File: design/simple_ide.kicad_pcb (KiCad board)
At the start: 4 copper layers, 41 x 100 mm, 14 parts, among them IC1 ATF22V10C-15PU, IC2 ATF22V10C-15PU, IC3 74ACT245, IC4 74ACT245, J2 Conn_02x22_Odd_Even

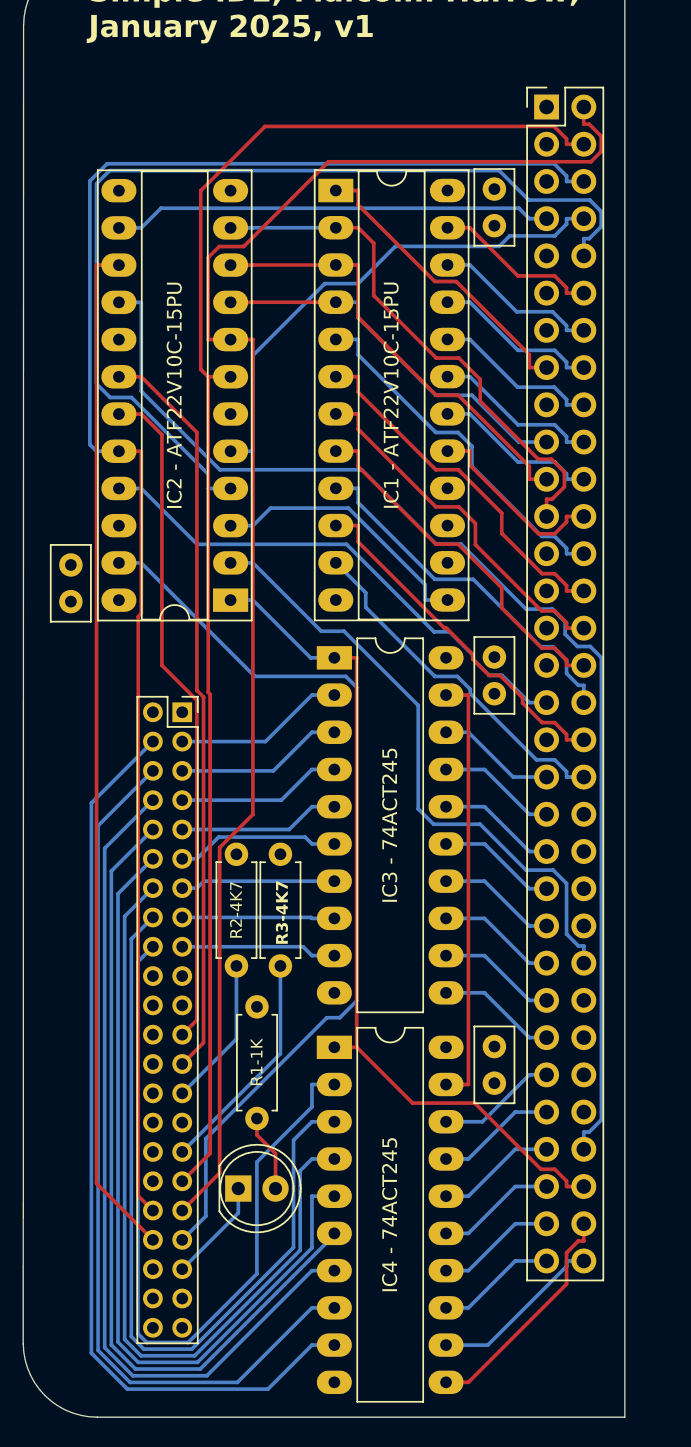
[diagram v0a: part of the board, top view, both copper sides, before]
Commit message: Recheck WinCUPL against design
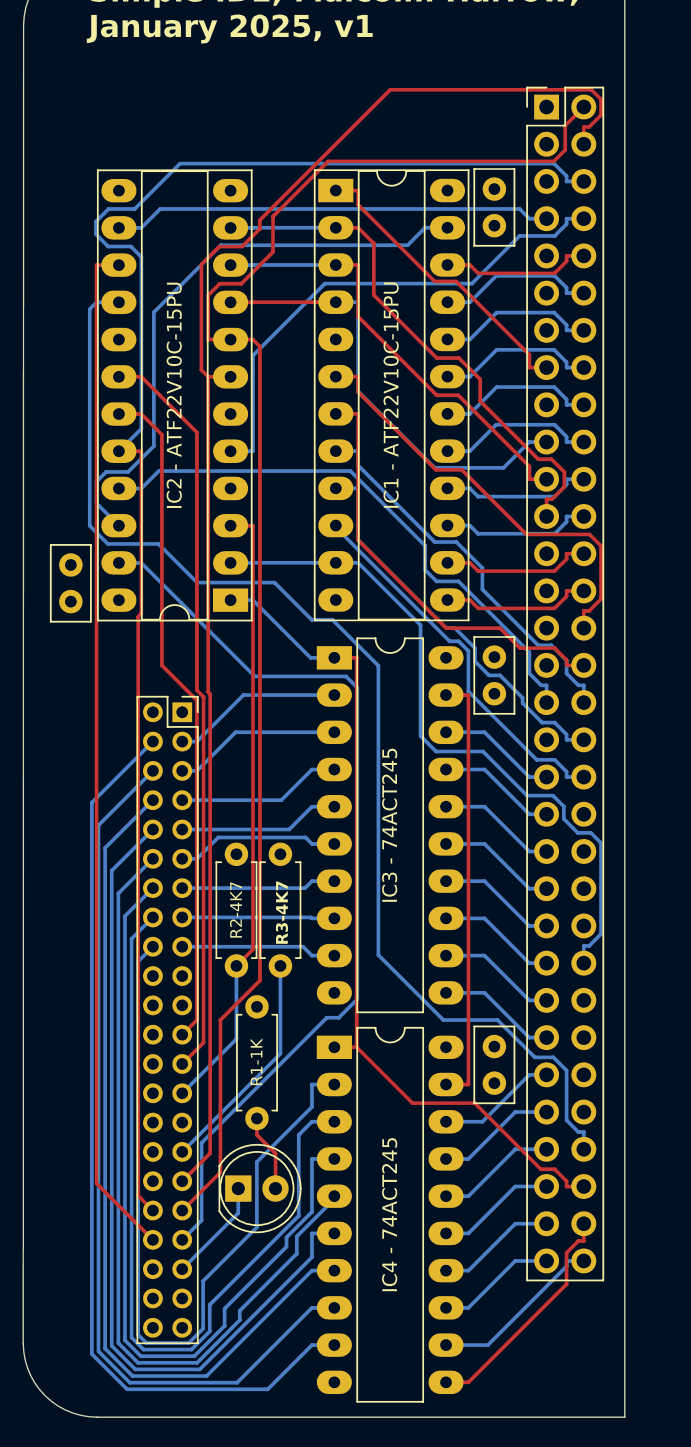
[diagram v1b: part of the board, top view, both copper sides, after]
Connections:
- IC1 pad 10: A18 -> A19
- IC1 pad 11: A19 -> AS
- IC1 pad 13: ~{IDECS} -> A14
- IC1 pad 14: unconnected-(IC1-I/O_1-Pad14) -> A13
- IC1 pad 15: unconnected-(IC1-I/O_2-Pad15) -> A12
- IC1 pad 16: unconnected-(IC1-I/O_3-Pad16) -> A11
- IC1 pad 17: A12 -> A10
- IC1 pad 18: A11 -> A9
- IC1 pad 19: A10 -> A8
- IC1 pad 20: A9 -> A7
- IC1 pad 21: A8 -> A6
- IC1 pad 22: A7 -> A5
- IC1 pad 23: A6 -> ~{IDECS}
- IC1 pad 5: A13 -> unconnected-(IC1-IN_3-Pad5)
- IC1 pad 6: A14 -> A15
- IC1 pad 7: A15 -> A16
- IC1 pad 8: A16 -> A17
- IC1 pad 9: A17 -> A18
- IC2 pad 22: unconnected-(IC2-I/O_9-Pad22) -> ~{IDECS}
- IC2 pad 3: ~{IDECS} -> IDERDY
- IC2 pad 4: A5 -> unconnected-(IC2-IN/PD-Pad4)
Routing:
- net A5: track 66.0 -> 10.2 mm
- net IDERDY: track 10.2 -> 42.3 mm
- net ~{IDECS}: track 18.5 -> 40.1 mm
- net A14: track 24.6 -> 10.2 mm
- net A13: track 24.6 -> 10.2 mm
- net A15: track 24.7 -> 29.8 mm
- net AS: track 42.3 -> 47.0 mm
- net A16: track 24.6 -> 29.3 mm
- net FC0: track 26.1 -> 30.6 mm
- net UDS: track 35.4 -> 38.7 mm
- net A2: track 98.8 -> 101.7 mm
- net A18: track 24.2 -> 27.0 mm
- net A12: track 12.9 -> 10.2 mm
- net A1: track 103.6 -> 101.2 mm
- net A19: track 23.9 -> 25.9 mm
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
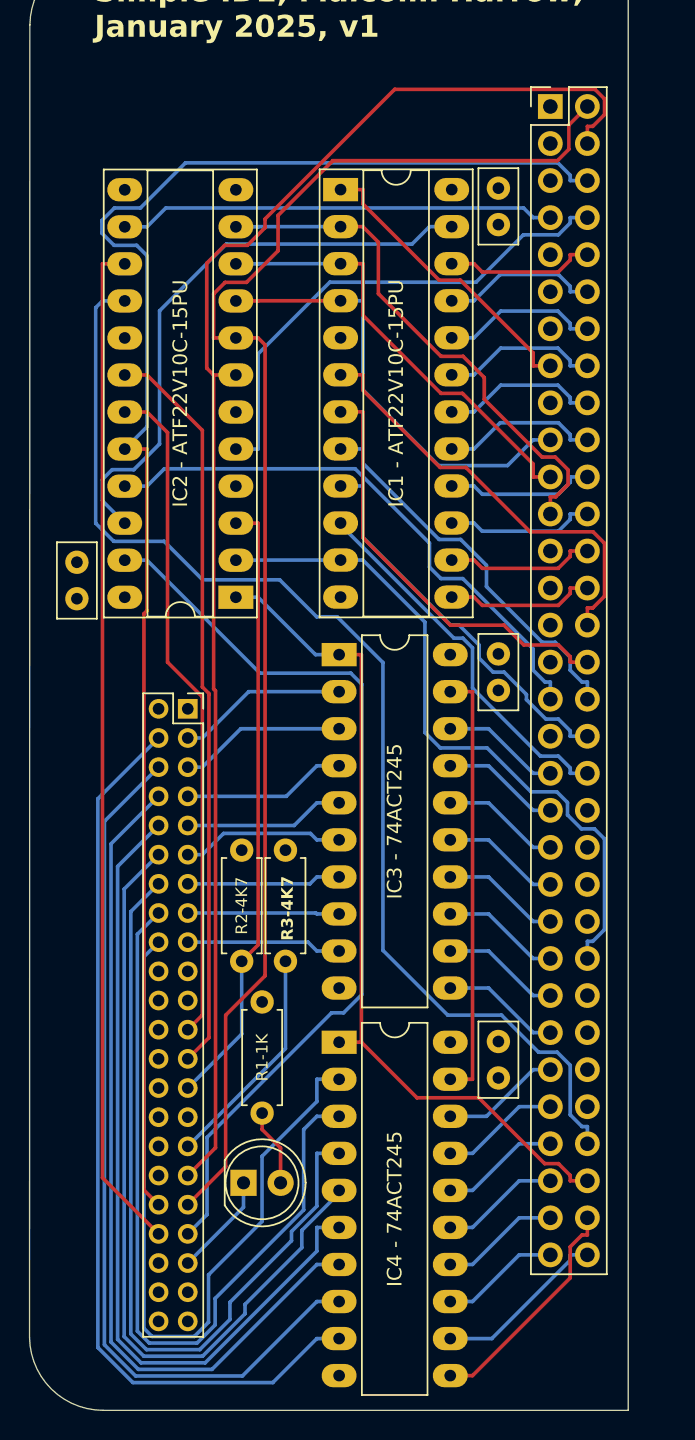
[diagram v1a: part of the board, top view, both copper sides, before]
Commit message: Compile Wincuple and reroute pins to ensure outputs on output pins
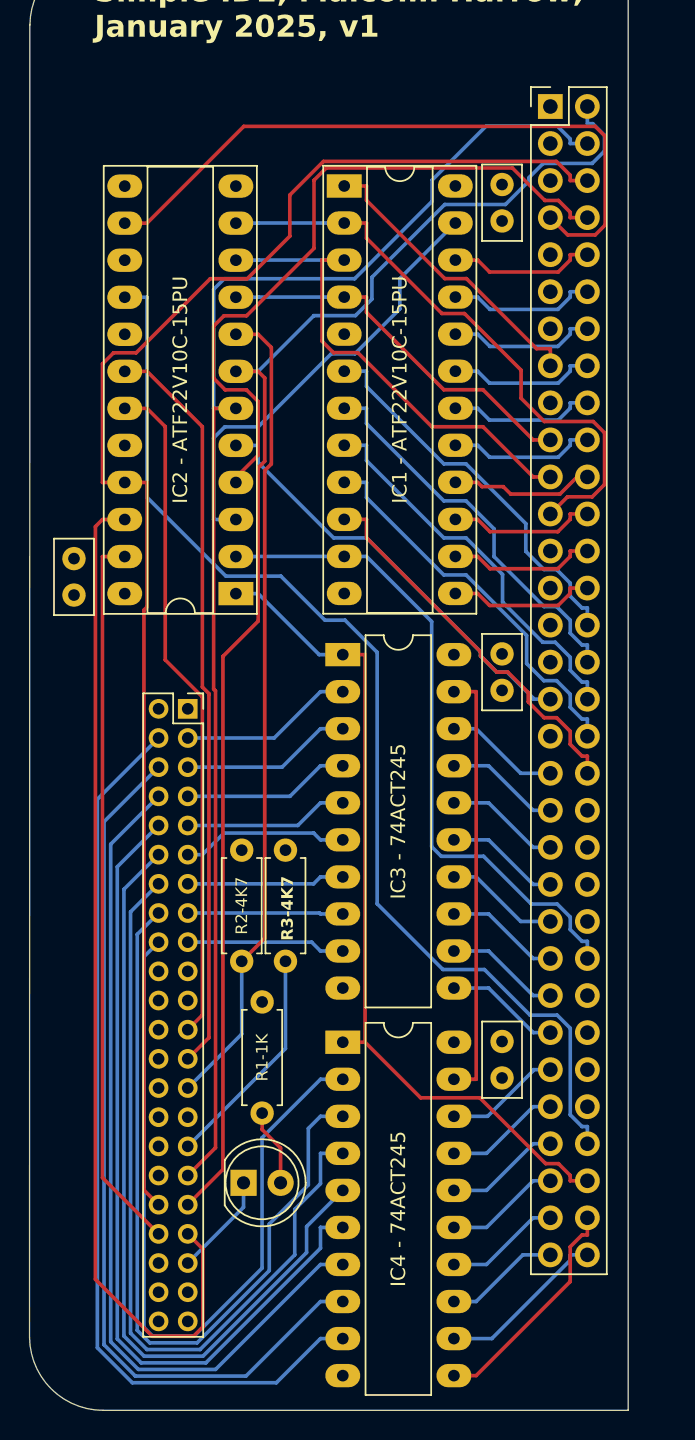
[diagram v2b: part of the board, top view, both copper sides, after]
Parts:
- moved C4 0.35 mm to (175.3, 51.0)
- moved IC1 0.35 mm to (164.5, 51.0)
- moved C3 0.32 mm to (146.0, 79.1)
- moved C1 0.25 mm to (175.3, 109.7)
- moved C2 0.25 mm to (175.3, 83.1)
- moved IC2 0.25 mm to (157.1, 79.0)
- moved IC3 0.25 mm to (164.4, 83.2)
- moved IC4 0.25 mm to (164.4, 109.8)
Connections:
- IC2 pad 13: IDESEL -> unconnected-(IC2-IN_10-Pad13)
- IC2 pad 15: ~{IDECS1} -> unconnected-(IC2-I/O_2-Pad15)
- IC2 pad 20: A3 -> IDESEL
- IC2 pad 21: UDS -> A3
- IC2 pad 22: ~{IDECS} -> ~{IDECS0}
- IC2 pad 23: ~{IDECS0} -> ~{IDECS1}
- IC2 pad 3: IDERDY -> ~{IDECS}
- IC2 pad 4: unconnected-(IC2-IN/PD-Pad4) -> A4
- IC2 pad 5: A4 -> UDS
- IC2 pad 6: unconnected-(IC2-IN_4-Pad6) -> A2
- IC2 pad 7: A2 -> A1
- IC2 pad 8: A1 -> IDERDY
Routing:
- net ~{IDECS1}: track 69.6 -> 49.6 mm
- net VPA: track 30.0 -> 46.6 mm
- net IDERDY: track 42.3 -> 56.0 mm
- net A4: track 34.7 -> 47.9 mm
- net ~{IDECS}: track 40.1 -> 31.0 mm
- net UDS: track 38.7 -> 29.7 mm
- net ~{IDECS0}: track 62.9 -> 69.9 mm
- net A3: track 108.0 -> 102.6 mm
- net A2: track 101.7 -> 96.5 mm
- net FC2: track 36.4 -> 41.1 mm
- net DTACK: track 82.5 -> 78.1 mm
- net FC0: track 30.6 -> 26.2 mm
- net A1: track 101.2 -> 97.3 mm
- net FC1: track 30.2 -> 34.0 mm
- net A15: track 29.8 -> 26.8 mm
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
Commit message: Start work on v2
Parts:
- removed D2: LED, LED_THT:LED_D5.0mm
- removed R1: 1K, Resistor_THT:R_Axial_DIN0207_L6.3mm_D2.5mm_P7.62mm_Horizontal
- removed R2, R3: 4K7, Resistor_THT:R_Axial_DIN0207_L6.3mm_D2.5mm_P7.62mm_Horizontal
- IC3, IC4: value 74ACT245 -> 74245
- moved C3 31.8 mm to (160.7, 51.0), turned to -90 degrees
- moved IC2 28.9 mm to (149.6, 51.0), turned to 0 degrees
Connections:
- IC2 pad 10: FC1 -> unconnected-(IC2-IN_8-Pad10)
- IC2 pad 11: FC2 -> unconnected-(IC2-IN_9-Pad11)
- IC2 pad 13: unconnected-(IC2-IN_10-Pad13) -> A2
- IC2 pad 14: VPA -> A1
- IC2 pad 6: A2 -> unconnected-(IC2-IN_4-Pad6)
- IC2 pad 7: A1 -> unconnected-(IC2-IN_5-Pad7)
- IC2 pad 8: IDERDY -> unconnected-(IC2-IN_6-Pad8)
- IC2 pad 9: FC0 -> unconnected-(IC2-IN_7-Pad9)
- IC3 pad 19: IDEBUF -> ~{IDEBUF}
- IC4 pad 19: IDEBUF -> ~{IDEBUF}
- J2 pad 1: ~{RESET} -> RESET
- J2 pad 27: IDERDY -> unconnected-(J2-Pin_27-Pad27)
- J2 pad 31: INTRQ -> unconnected-(J2-Pin_31-Pad31)
- J2 pad 39: ~{DASP} -> unconnected-(J2-Pin_39-Pad39)
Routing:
- net RESET: track 0.00 -> 69.3 mm, vias 0 -> 1
- net IDERDY: track 56.0 -> 0.00 mm
- net ~{IDEBUF}: track 0.00 -> 54.3 mm
- net VPA: track 46.6 -> 0.00 mm
- net RW: track 58.1 -> 92.4 mm
- net IDEBUF: track 29.6 -> 0.00 mm
- net A1: track 97.3 -> 126.8 mm
- net AS: track 45.8 -> 71.9 mm
- net ~{IDECS1}: track 49.6 -> 73.7 mm
- net DTACK: track 78.1 -> 59.7 mm
- net INTRQ: track 15.5 -> 0.00 mm
- net A2: track 96.5 -> 111.6 mm
- net FC2: track 41.1 -> 27.8 mm
- net UDS: track 29.7 -> 42.2 mm
- net A3: track 102.6 -> 94.1 mm
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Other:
- board text added: "< 1"
- board text added: "DID YOU CHANGE A2 and A1 in PLD ???"
- board text added: "IC1"
- board text added: "IC2"
- board text added: "KEY --->"
- board text added: "Simple IDE, Malcolm Harrow, February 2025, v2"
- board text removed: "Simple IDE, Malcolm Harrow, January 2025, v1"

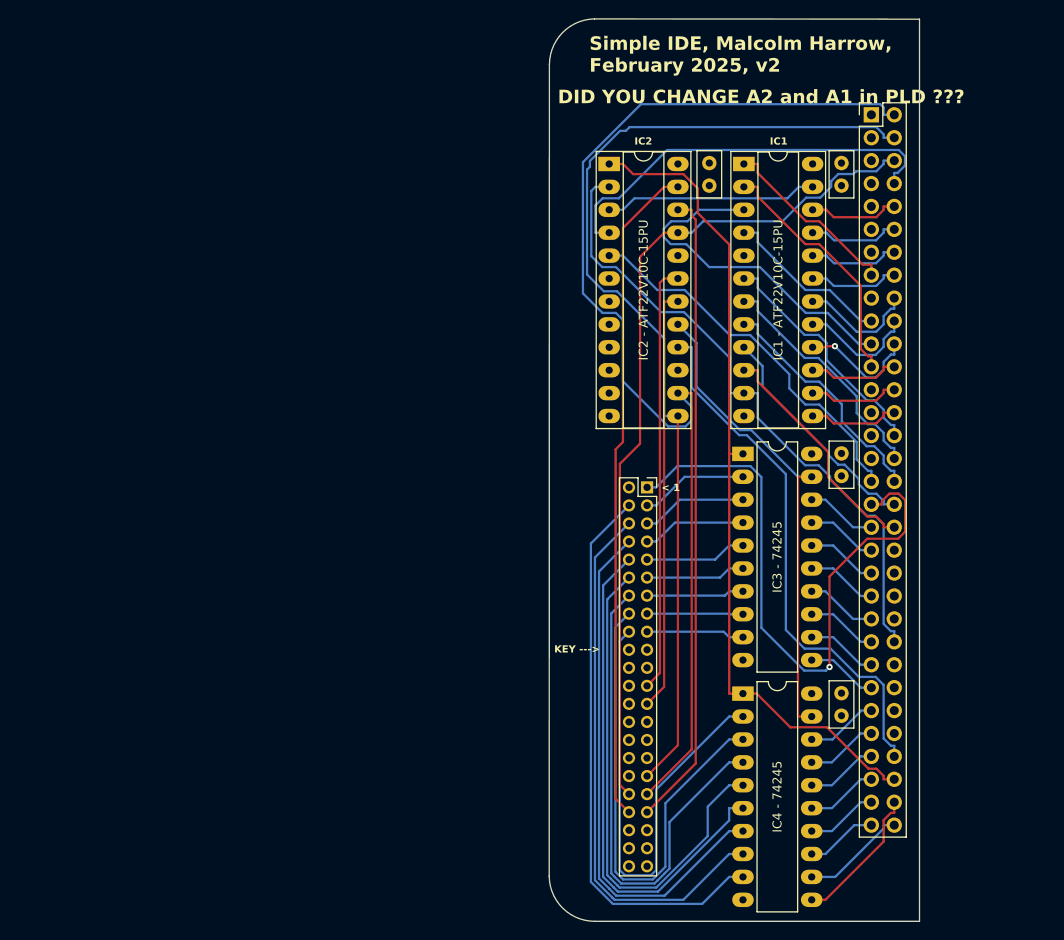
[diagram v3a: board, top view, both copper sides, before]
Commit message: First test of v2 production files .. seems to read a disk ok
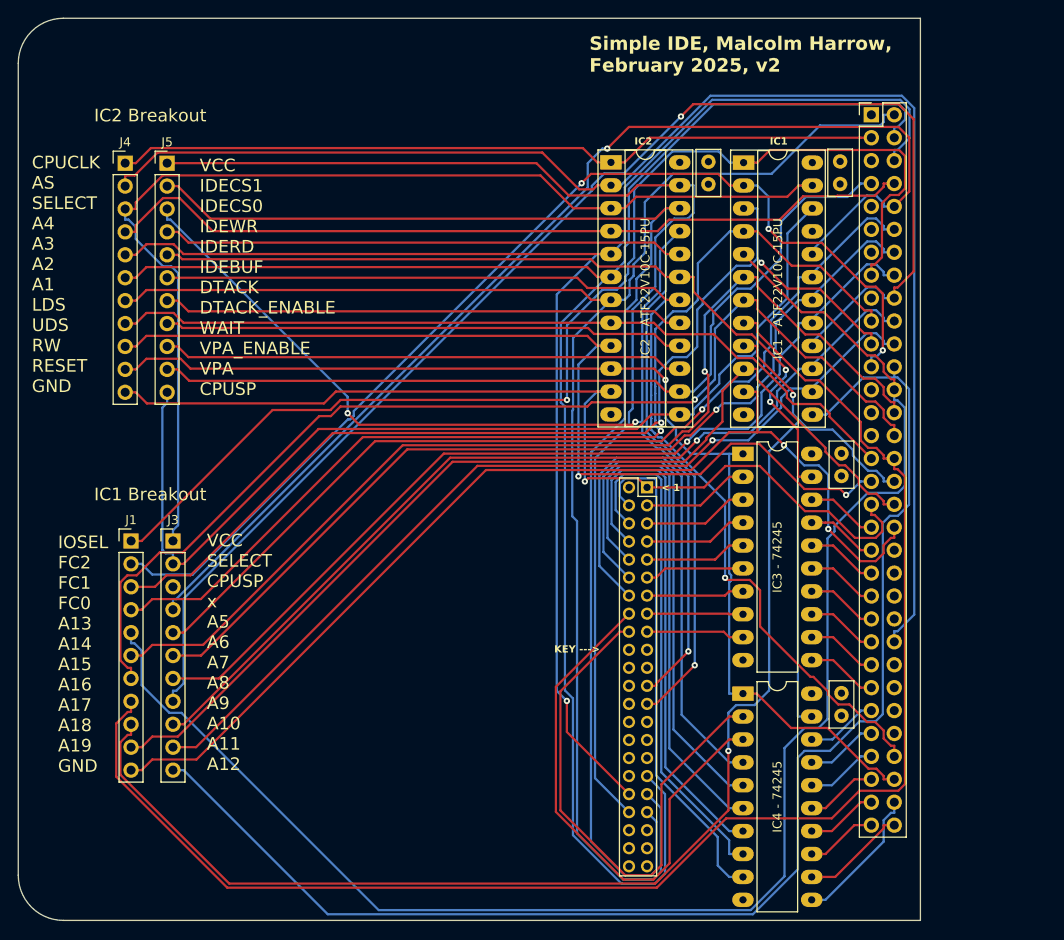
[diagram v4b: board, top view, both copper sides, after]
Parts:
- added J1: Conn_01x11_Pin, Connector_PinHeader_2.54mm:PinHeader_1x11_P2.54mm_Vertical, F.Cu at (96.6, 92.8)
- added J3: Conn_01x11_Pin, Connector_PinHeader_2.54mm:PinHeader_1x11_P2.54mm_Vertical, F.Cu at (101.2, 92.8)
- added J4: Conn_01x11_Pin, Connector_PinHeader_2.54mm:PinHeader_1x11_P2.54mm_Vertical, F.Cu at (96.0, 51.0)
- added J5: Conn_01x11_Pin, Connector_PinHeader_2.54mm:PinHeader_1x11_P2.54mm_Vertical, F.Cu at (100.6, 51.0)
- moved IC2 0.27 mm to (149.8, 50.9)
- moved C4 0.23 mm to (175.2, 50.8)
- moved C3 0.18 mm to (160.6, 50.8)
- moved IC1 0.15 mm to (164.5, 50.9)
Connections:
- net ~{IDECS} renamed SELECT
- IC1 pad 10: A19 -> A18
- IC1 pad 11: AS -> A19
- IC1 pad 13: A14 -> A12
- IC1 pad 14: A13 -> A11
- IC1 pad 15: A12 -> A10
- IC1 pad 16: A11 -> A9
- IC1 pad 17: A10 -> A8
- IC1 pad 18: A9 -> A7
- IC1 pad 19: A8 -> A6
- IC1 pad 20: A7 -> A5
- IC1 pad 21: A6 -> unconnected-(IC1-I/O_8-Pad21)
- IC1 pad 22: A5 -> CPUSP
- IC1 pad 5: unconnected-(IC1-IN_3-Pad5) -> A13
- IC1 pad 6: A15 -> A14
- IC1 pad 7: A16 -> A15
- IC1 pad 8: A17 -> A16
- IC1 pad 9: A18 -> A17
- IC2 pad 1: RW -> CPUCLK
- IC2 pad 10: unconnected-(IC2-IN_8-Pad10) -> RW
- IC2 pad 11: unconnected-(IC2-IN_9-Pad11) -> RESET
- IC2 pad 13: A2 -> CPUSP
- IC2 pad 14: A1 -> VPA
- IC2 pad 15: unconnected-(IC2-I/O_2-Pad15) -> VPA_ENABLE
- IC2 pad 16: DTACK -> WAIT
- IC2 pad 17: ~{IDEBUF} -> DTACK_ENABLE
- IC2 pad 18: ~{IDERD} -> DTACK
- IC2 pad 19: ~{IDEWR} -> ~{IDEBUF}
- IC2 pad 20: IDESEL -> ~{IDERD}
- IC2 pad 21: A3 -> ~{IDEWR}
- IC2 pad 5: UDS -> A3
- IC2 pad 6: unconnected-(IC2-IN_4-Pad6) -> A2
- IC2 pad 7: unconnected-(IC2-IN_5-Pad7) -> A1
- IC2 pad 8: unconnected-(IC2-IN_6-Pad8) -> LDS
- IC2 pad 9: unconnected-(IC2-IN_7-Pad9) -> UDS
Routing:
- net A13: track 10.1 -> 176.8 mm
- net A12: track 10.1 -> 153.7 mm
- net A16: track 26.8 -> 168.3 mm
- net A9: track 13.2 -> 150.4 mm, vias 0 -> 1
- net A17: track 26.8 -> 155.3 mm, vias 0 -> 2
- net A5: track 10.1 -> 127.6 mm, vias 0 -> 1
- net CPUSP: track 0.00 -> 113.9 mm
- net IOSEL: track 20.5 -> 130.8 mm, vias 0 -> 1
- net A14: track 10.1 -> 116.8 mm, vias 0 -> 1
- net SELECT: track 23.6 -> 120.9 mm
- net FC0: track 18.8 -> 114.1 mm, vias 0 -> 1
- net VPA: track 0.00 -> 94.8 mm
- net A15: track 26.8 -> 121.4 mm, vias 0 -> 1
- net A8: track 10.1 -> 103.5 mm, vias 0 -> 1
- net A6: track 10.1 -> 103.5 mm, vias 0 -> 1
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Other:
- board size 41 x 100 mm -> 100 x 100 mm
- board text added: "CPUCLK AS SELECT A4 A3 A2 A1 LDS UDS RW RESET GND"
- board text added: "IC1 Breakout"
- board text added: "IC2 Breakout"
- board text added: "IOSEL FC2 FC1 FC0 A13 A14 A15 A16 A17 A18 A19 GND"
- board text added: "VCC IDECS1 IDECS0 IDEWR IDERD IDEBUF DTACK DTACK_ENABLE WAIT VPA_ENABLE VPA CPUSP"
- board text added: "VCC SELECT CPUSP x A5 A6 A7 A8 A9 A10 A11 A12"
- board text removed: "DID YOU CHANGE A2 and A1 in PLD ???"

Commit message: Save copy of firmware
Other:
- board text added: "A1"
- board text added: "A10"
- board text added: "A11"
- board text added: "A12"
- board text added: "A13"
- board text added: "A14"
- board text added: "A15"
- board text added: "A16"
- board text added: "A17"
- board text added: "A18"
- board text added: "A19"
- board text added: "A2"
- board text added: "A3"
- board text added: "A4"
- board text added: "A5"
- board text added: "A6"
- board text added: "A7"
- board text added: "A8"
- board text added: "A9"
- board text added: "AS"
- board text added: "CPUCLK"
- board text added: "CPUSP"
- board text added: "DTACK"
- board text added: "DTACK_ENABLE"
- board text added: "FC0"
- board text added: "FC1"
- board text added: "FC2"
- board text added: "IDEBUF"
- board text added: "IDECS0"
- board text added: "IDECS1"
- board text added: "IDERD"
- board text added: "IDEWR"
- board text added: "IOSEL"
- board text added: "LDS"
- board text added: "RESET"
- board text added: "RW"
- board text added: "SELECT"
- board text added: "Simple IDE, Malcolm Harrow, March 2025, v2.1"
- board text added: "UDS"
- board text added: "VPA"
- board text added: "VPA_ENABLE"
- board text added: "WAIT"
- board text added: "X"
- board text removed: "CPUCLK AS SELECT A4 A3 A2 A1 LDS UDS RW RESET GND"
- board text removed: "IOSEL FC2 FC1 FC0 A13 A14 A15 A16 A17 A18 A19 GND"
- board text removed: "Simple IDE, Malcolm Harrow, February 2025, v2"
- board text removed: "VCC IDECS1 IDECS0 IDEWR IDERD IDEBUF DTACK DTACK_ENABLE WAIT VPA_ENABLE VPA CPUSP"
- board text removed: "VCC SELECT CPUSP x A5 A6 A7 A8 A9 A10 A11 A12"
